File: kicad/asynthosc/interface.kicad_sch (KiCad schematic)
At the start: 2 parts, among them SW4 SW_MEC_5G_LED

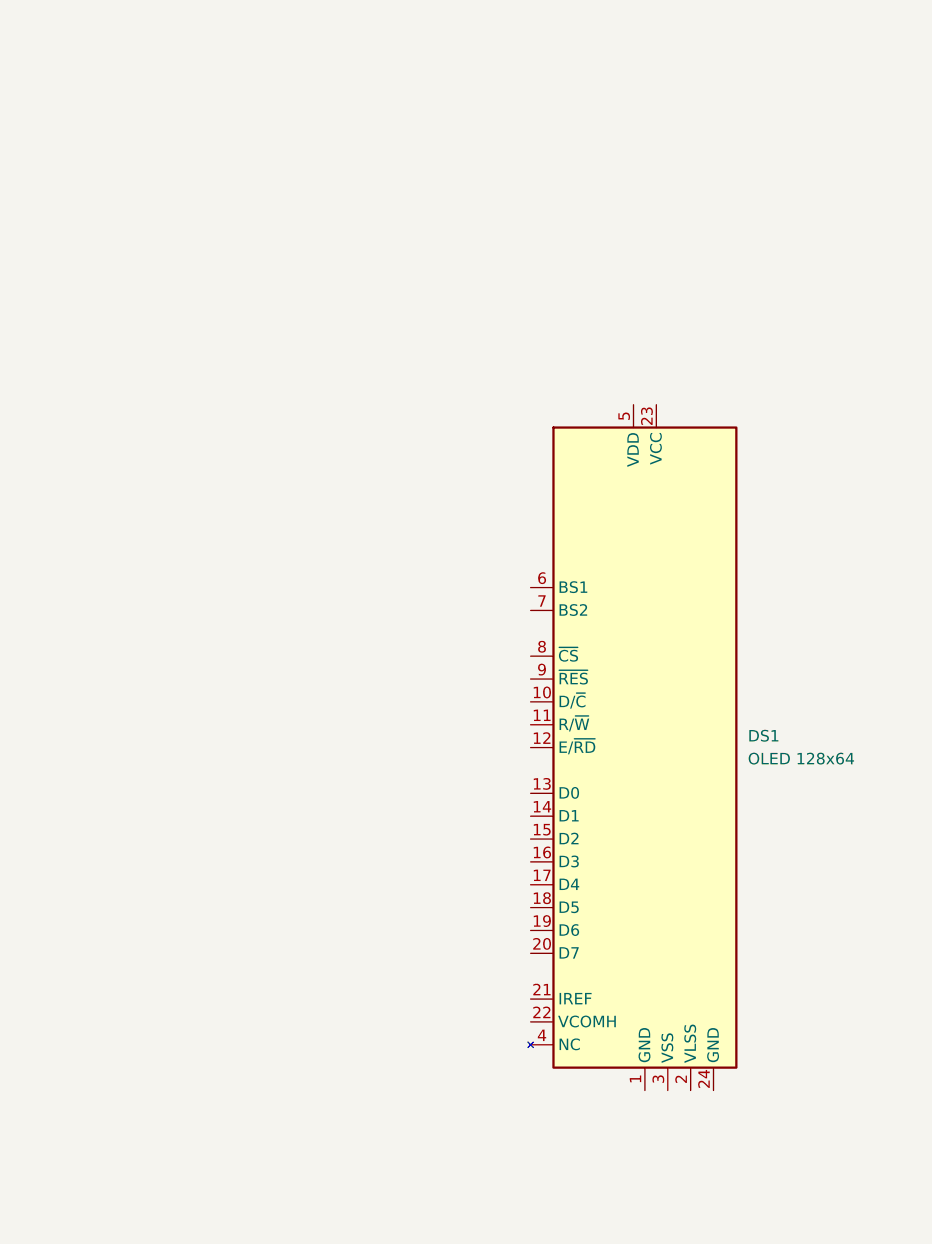
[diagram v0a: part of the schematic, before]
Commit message: sch: add spi nor, display connection, and more footprints
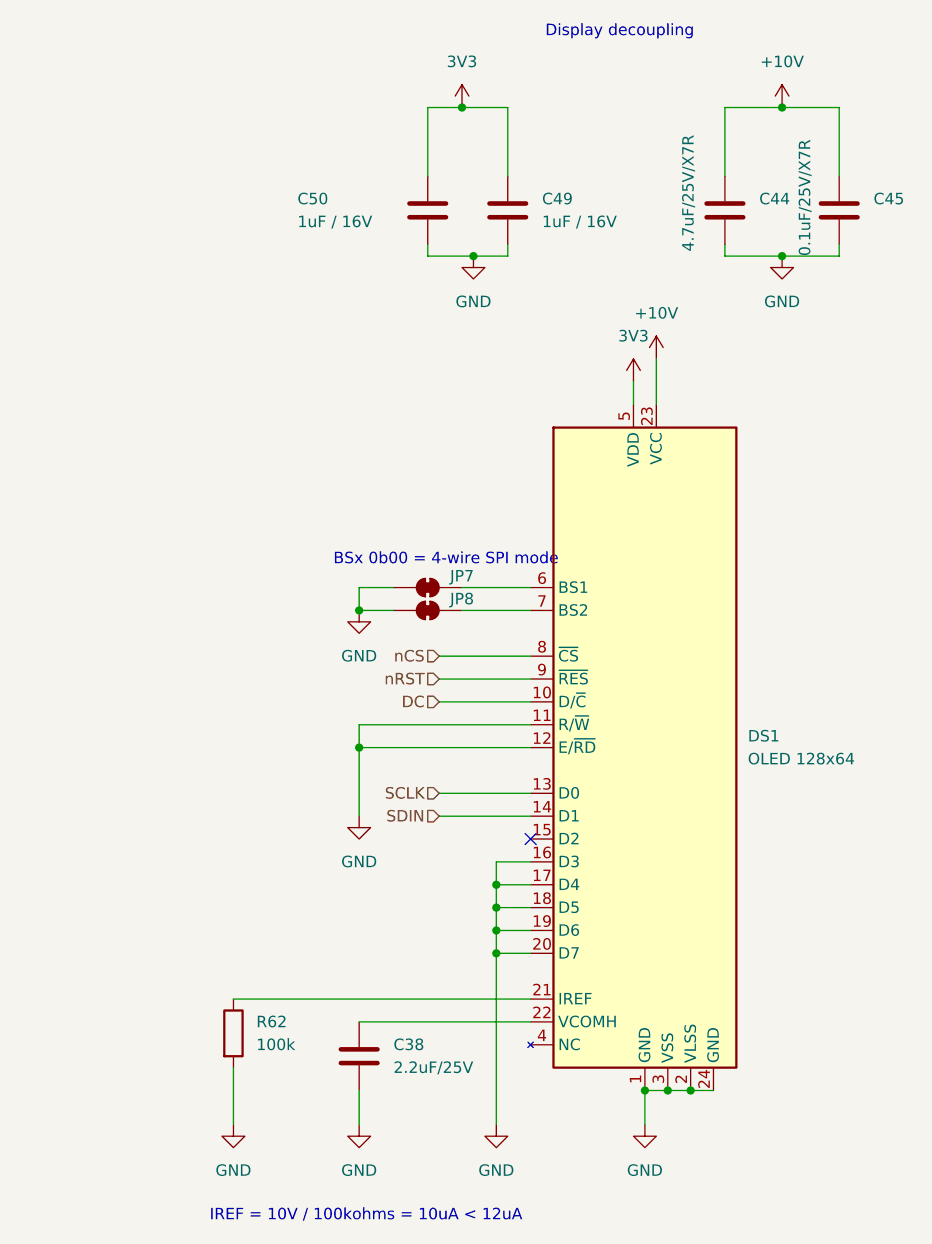
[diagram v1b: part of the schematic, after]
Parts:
- added C38: 2.2uF/25V, symbol Device:C
- added C44: 4.7uF/25V/X7R, symbol Device:C
- added C45: 0.1uF/25V/X7R, symbol Device:C
- added C49, C50: 1uF / 16V, 0805, symbol Device:C
- added JP7, JP8: SolderJumper_2_Bridged, symbol Jumper:SolderJumper_2_Bridged
- added R62: 100k, symbol Device:R
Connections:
- net GND: now reaches DS1.1 (GND)
- net GND: now also DS1.11 (R/~{W}), DS1.12 (E/~{RD}), DS1.16 (D3), DS1.17 (D4), DS1.18 (D5), DS1.19 (D6), DS1.2 (VLSS), DS1.20 (D7), DS1.24 (GND), DS1.3 (VSS), C38.2, C44.2, C45.2, C49.2, C50.2, JP7.1 (A), JP8.1 (A), R62.2
- net DC: now reaches DS1.10 (D/~{C})
- net SCLK: now reaches DS1.13 (D0)
- net SDIN: now reaches DS1.14 (D1)
- net at DS1.21 (IREF): now also R62.1
- net at DS1.22 (VCOMH): now also C38.1
- net +10V: now reaches DS1.23 (VCC)
- net +10V: now also C44.1, C45.1
- net 3V3: now reaches DS1.5 (VDD)
- net 3V3: now also C49.1, C50.1
- net at DS1.6 (BS1): now also JP7.2 (B)
- net at DS1.7 (BS2): now also JP8.2 (B)
- net nCS: now reaches DS1.8 (~{CS})
- net nRST: now reaches DS1.9 (~{RES})
- no-connect marks 0 -> 1
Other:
- note added: "BSx 0b00 = 4-wire SPI mode"
- note added: "Display decoupling"
- note added: "IREF = 10V / 100kohms = 10uA < 12uA"

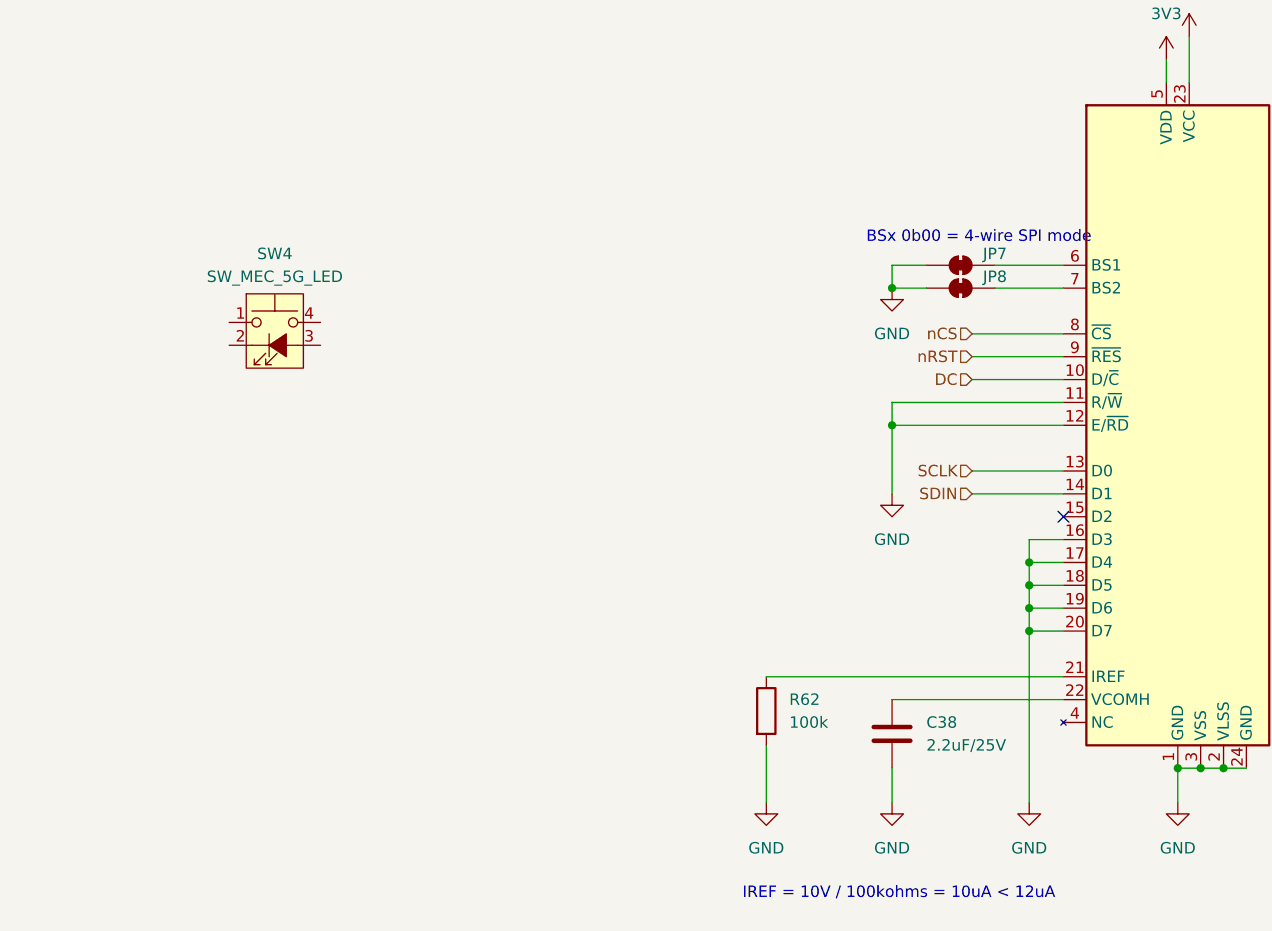
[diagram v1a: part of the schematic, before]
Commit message: sch: update footprint links
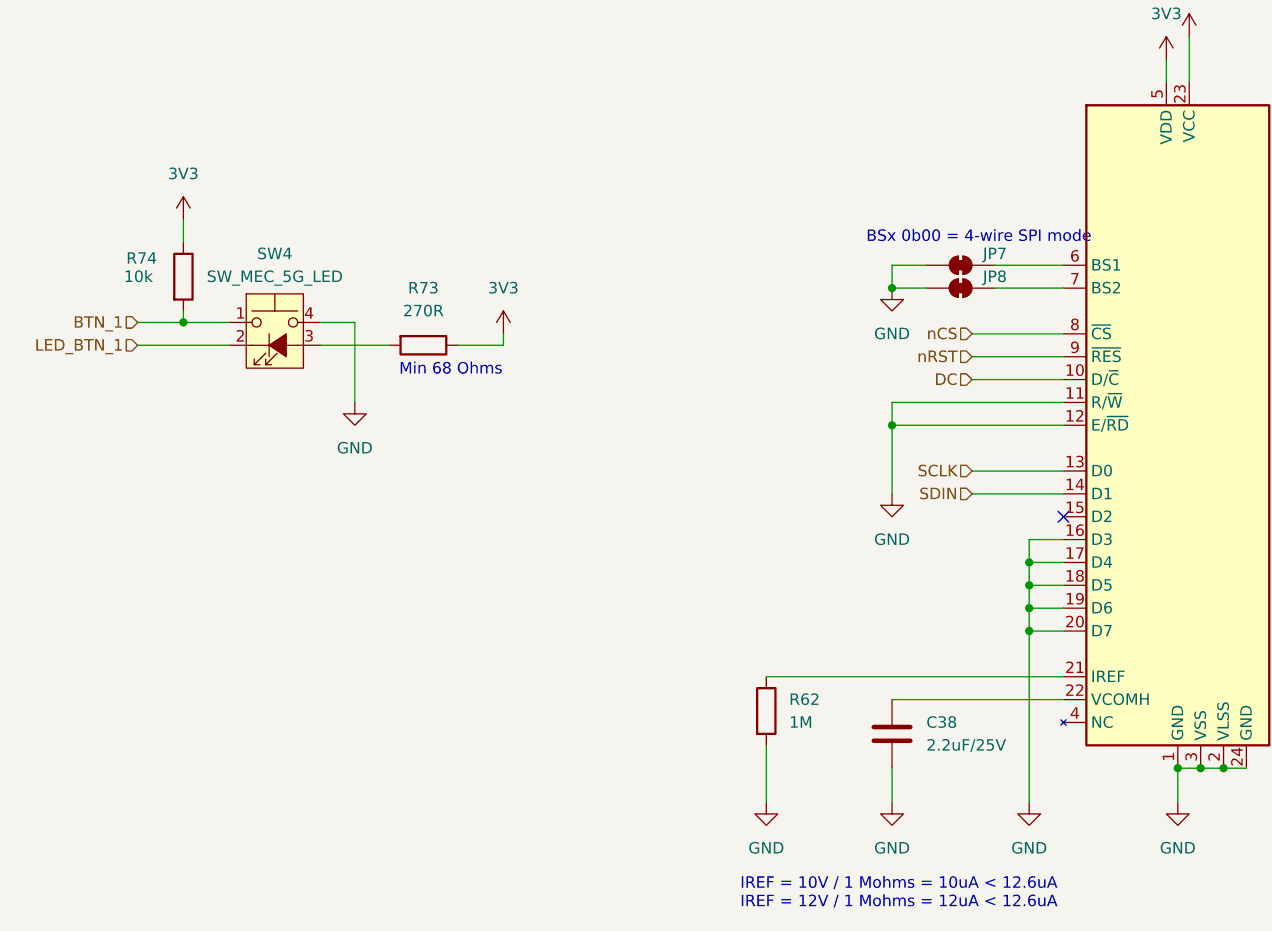
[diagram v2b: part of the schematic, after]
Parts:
- added R73: 270R, Resistor_SMD:R_0402_1005Metric, symbol Device:R
- added R74: 10k, Resistor_SMD:R_0402_1005Metric, symbol Device:R
- C38, C44, C45: footprint (none) -> Capacitor_SMD:C_0805_2012Metric
- C49, C50: footprint 0805 -> Capacitor_SMD:C_0805_2012Metric
- JP7, JP8: footprint (none) -> Jumper:SolderJumper-2_P1.3mm_Bridged2Bar_Pad1.0x1.5mm
- R62: value 100k -> 1M; footprint (none) -> Resistor_SMD:R_0402_1005Metric
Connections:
- net 3V3: now also R73.1, R74.1
- net GND: now also SW4.4 (A)
- net BTN_1: now reaches SW4.1
- net BTN_1: now also R74.2
- net LED_BTN_1: now reaches SW4.2
- net at SW4.3 (K): now also R73.2
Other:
- note added: "IREF = 10V / 1 Mohms = 10uA < 12.6uA IREF = 12V / 1 Mohms = 12uA < 12.6uA"
- note added: "Min 68 Ohms"
- note removed: "IREF = 10V / 100kohms = 10uA < 12uA"

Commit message: wip
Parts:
- added C55, C56: 100n, Capacitor_SMD:C_0402_1005Metric, symbol Device:C
- added R75, R77, R78: 10k, Resistor_SMD:R_0402_1005Metric, symbol Device:R
- added R79: 270R, Resistor_SMD:R_0402_1005Metric, symbol Device:R
- added SW3: RotaryEncoder, Rotary_Encoder:RotaryEncoder_Alps_EC12E_Vertical_H20mm, symbol Device:RotaryEncoder
- added SW9: SW_MEC_5G_LED, asynthosc:TPB01-X0XLXX_SW_MEC_5G, symbol Switch:SW_MEC_5G_LED
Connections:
- net 3V3: now also R75.1, R77.1, R78.1, R79.1
- net GND: now also C55.2, C56.2, SW3.C, SW9.4 (A)
- new net: R79.2, SW9.3 (K)
- new net BTN_2: R78.2, SW9.1
- new net LED_BTN_2: SW9.2
- new net ROT_A: C56.1, R77.2, SW3.A
- new net ROT_B: C55.1, R75.2, SW3.B
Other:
- note added: "Alps EC11E18244AU"
- note added: "Rotary: https://www.lcsc.com/product-detail/Rotary-Encoders_ALPSALPINE-EC21A1520407_C127463.html Need to 3D print a piece"
- moved on the sheet: R73, R74, SW4

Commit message: sch: change stm32 for smaller one, create smaller jumper footprint
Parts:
- C38, C44, C45, C49, C50, C55, C56: RefNum (none) -> _generic_
- DS1: Manufacturer (none) -> HRO Parts; RefNum (none) -> FPC0.5B-WTG-24P
- JP7, JP8: footprint Jumper:SolderJumper-2_P1.3mm_Bridged2Bar_Pad1.0x1.5mm -> asynthosc:SolderJumper_0402_1005Metric_Bridged
- SW3: Manufacturer (none) -> Alps; RefNum Alps EC11E18244AU -> EC11E18244AU
- SW4, SW9: Manufacturer (none) -> ROCPU; RefNum (none) -> TPB01-3016L6W

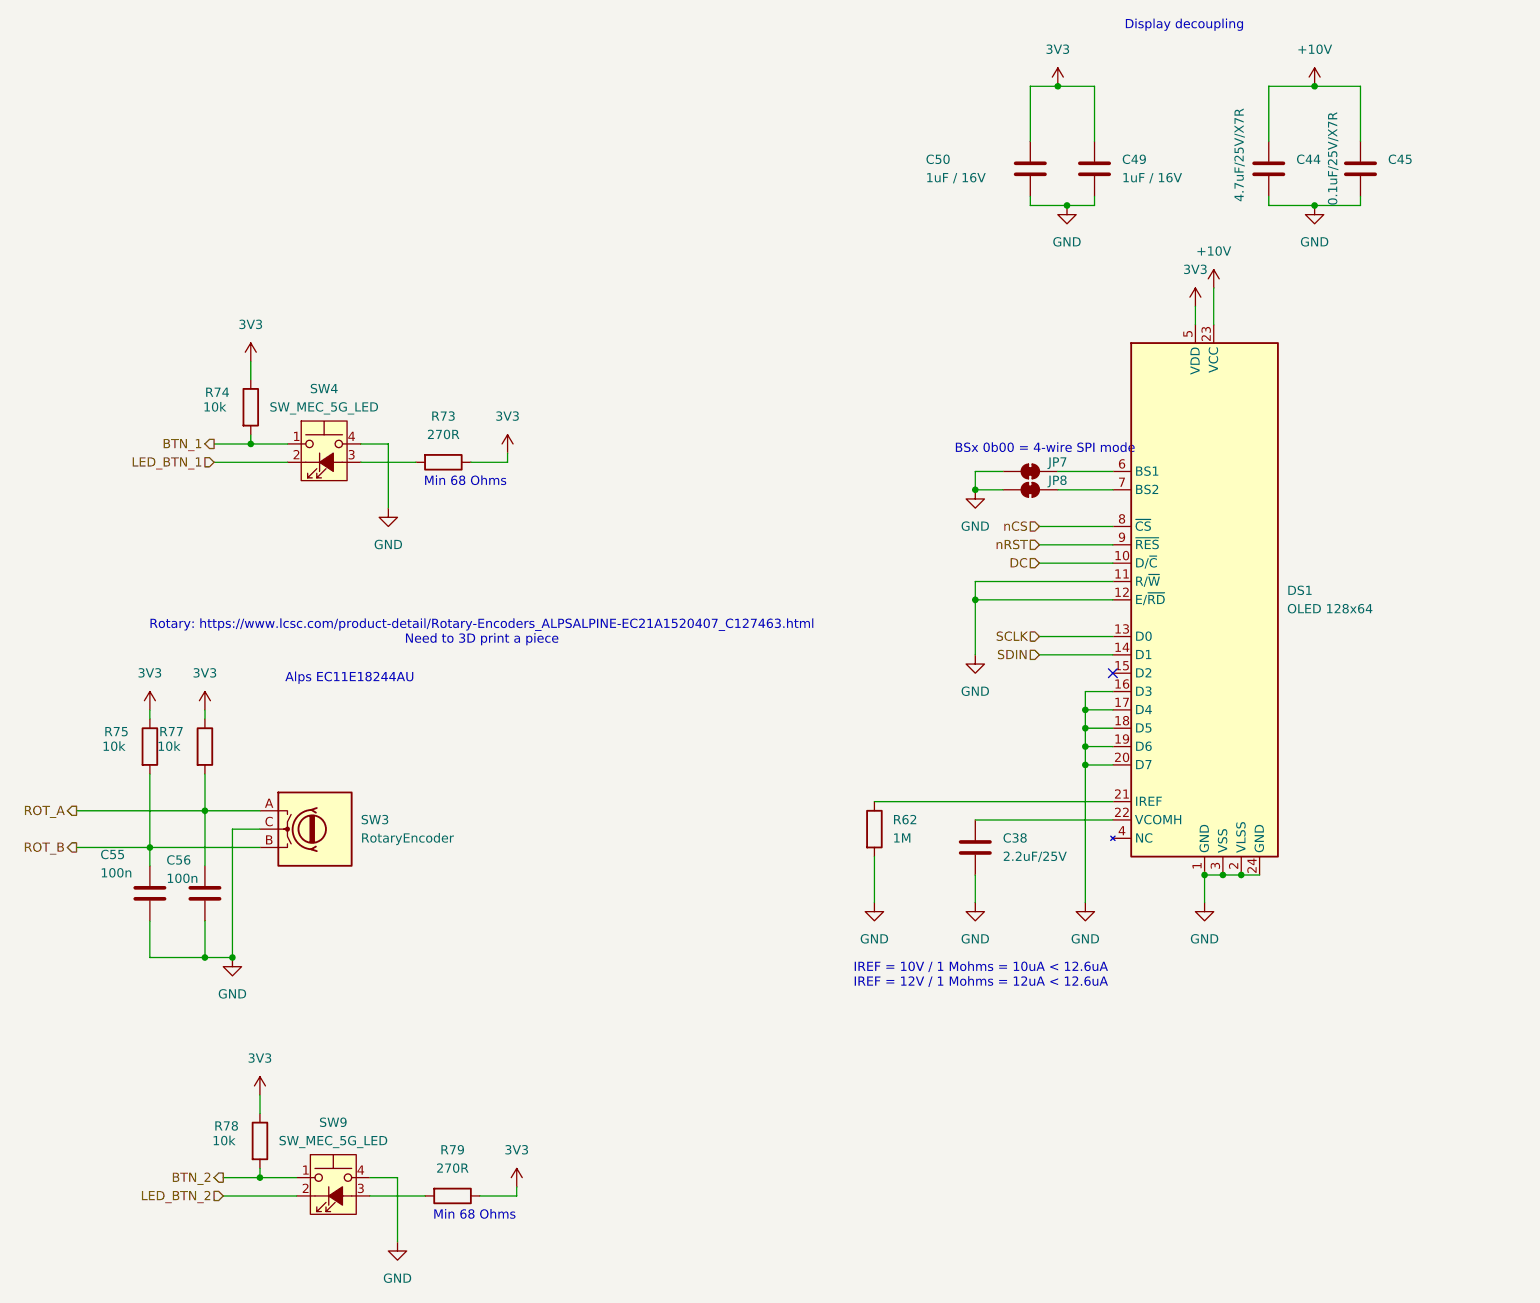
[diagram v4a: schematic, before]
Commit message: bom: update bom for lcsc
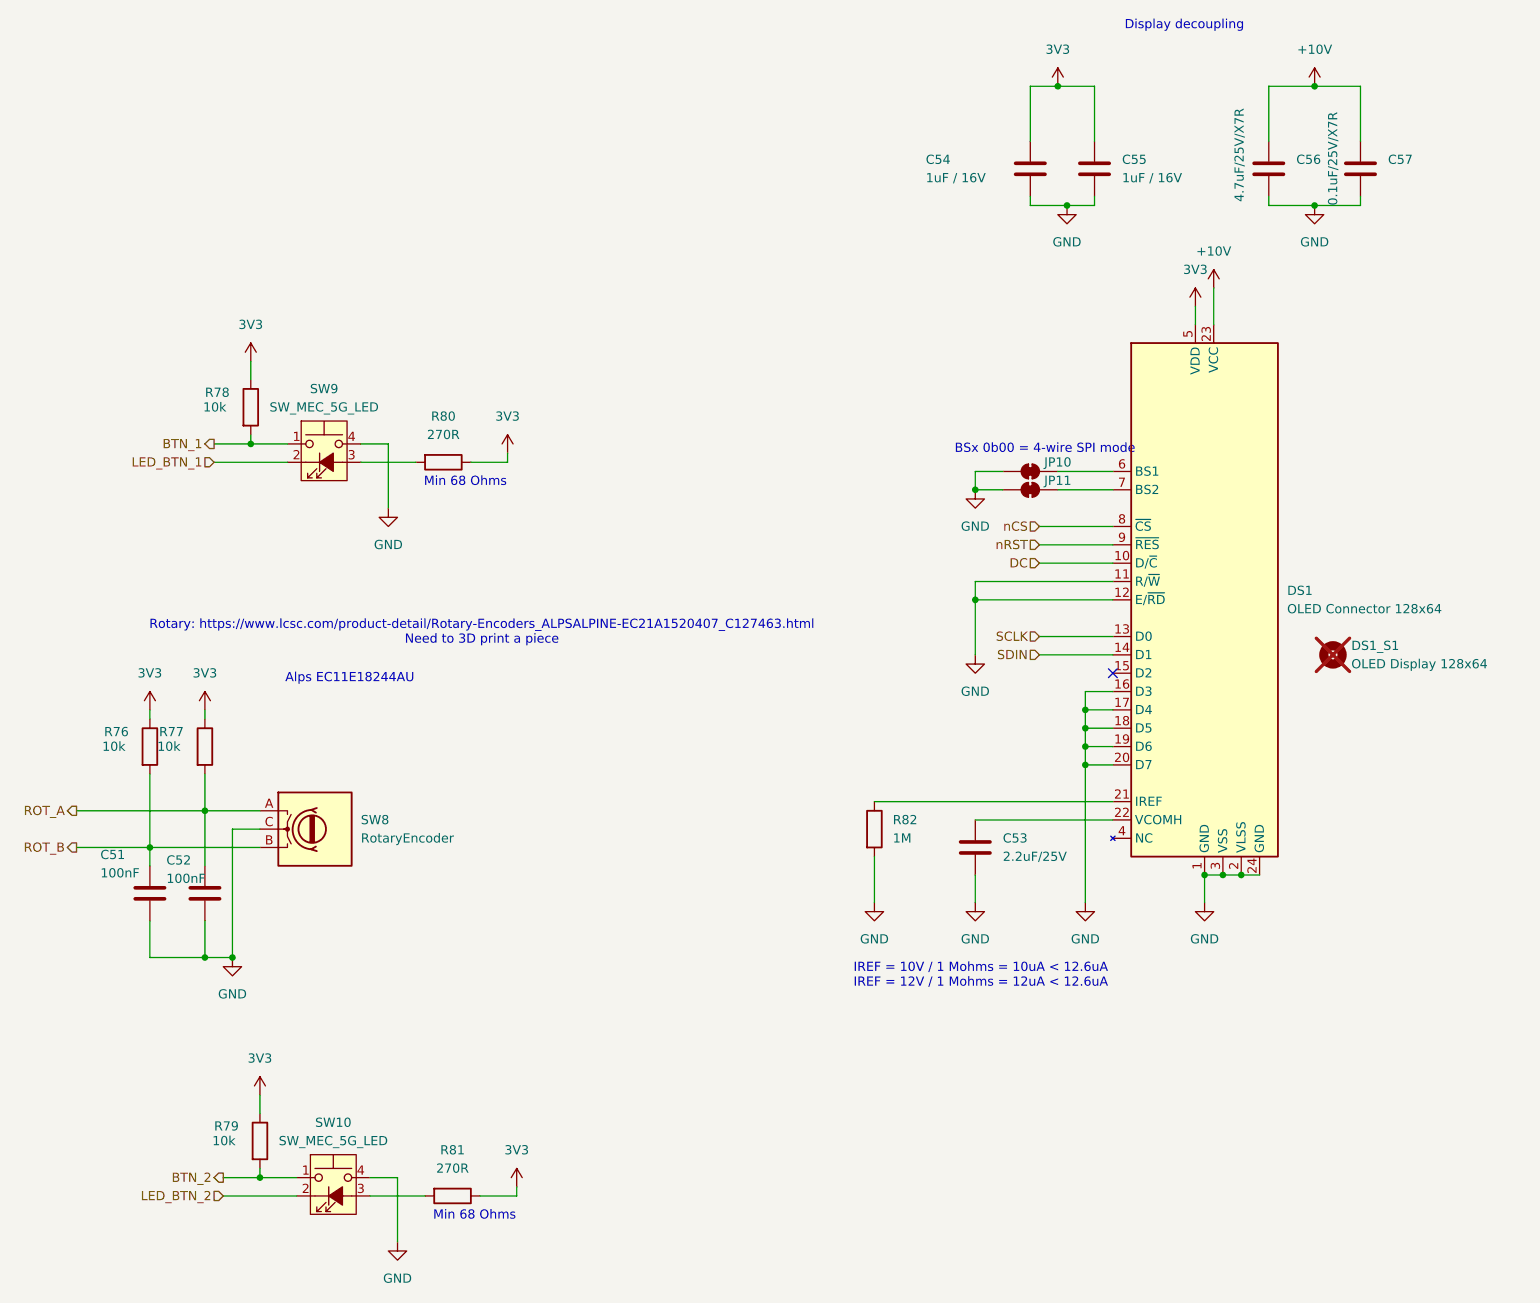
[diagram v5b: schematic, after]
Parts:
- added DS1_S1: OLED Display 128x64, Display:OLED-128O064D, symbol Mechanical:MountingHole
- C51: renamed from C55; value 100n -> 100nF
- C52: renamed from C56; value 100n -> 100nF
- DS1: value OLED 128x64 -> OLED Connector 128x64
- JP10: renamed from JP7; RefNum (none) -> _na_
- JP11: renamed from JP8; RefNum (none) -> _na_
- R76: renamed from R75; RefNum (none) -> _generic_
- R77: RefNum (none) -> _generic_
- R78: renamed from R74; RefNum (none) -> _generic_
- R79: renamed from R78; RefNum (none) -> _generic_
- R80: renamed from R73; RefNum (none) -> _generic_
- R81: renamed from R79; RefNum (none) -> _generic_
- R82: renamed from R62; RefNum (none) -> _generic_
- renumbered C38 to C53, C50 to C54, C49 to C55, C44 to C56, C45 to C57, SW9 to SW10, SW3 to SW8, SW4 to SW9
